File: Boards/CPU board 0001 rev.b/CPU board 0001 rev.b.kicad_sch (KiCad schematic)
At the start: 78 parts, among them J1 CEC card edge connector large, U10 7432, U11 7442, U12 7406, U13 7406, U14 7442, U15 7442, U16 M8216, U17 M8216, U18 6532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

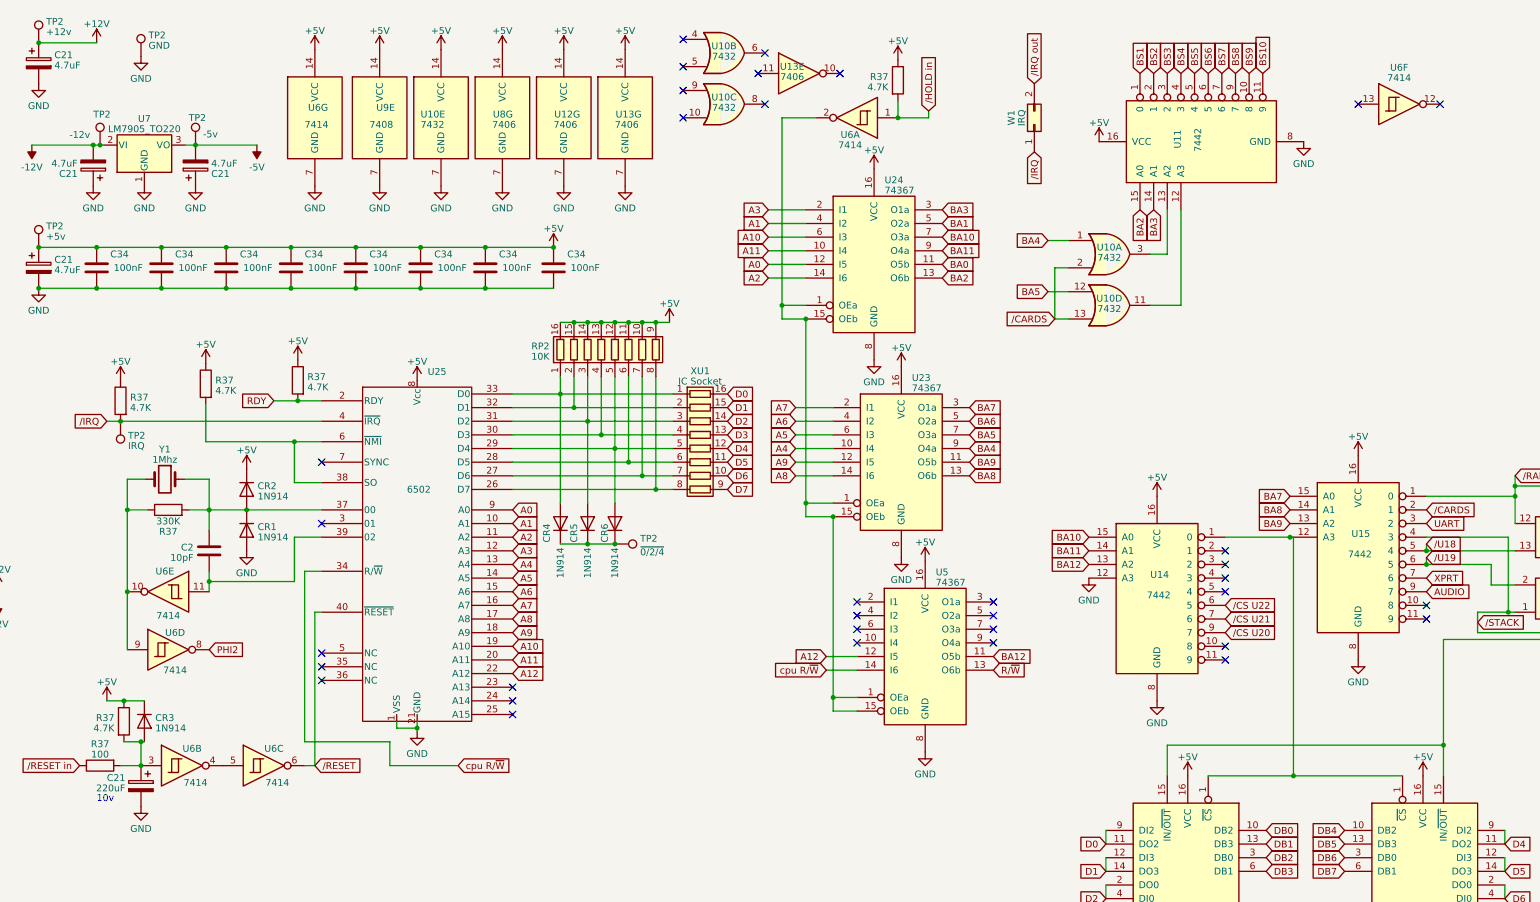
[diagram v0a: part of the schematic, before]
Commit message: checked Rev.c cpu board and tweaked copper on a and b
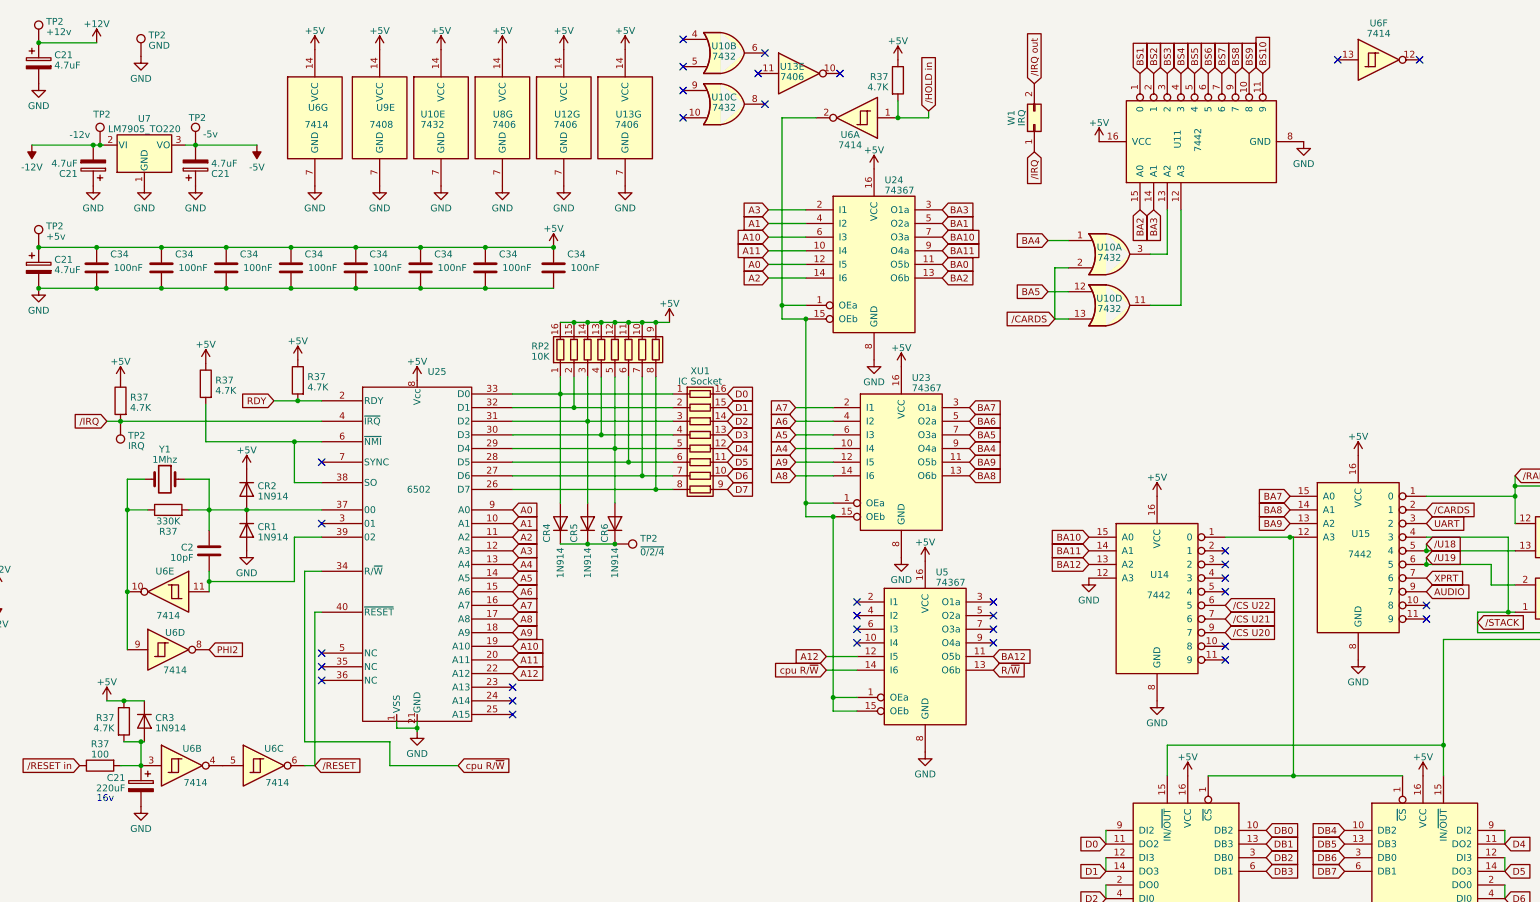
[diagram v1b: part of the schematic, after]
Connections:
- net at U18.18 (PB5): now also U12.3
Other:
- note added: "16v"
- note removed: "10v"
- moved on the sheet: U6F

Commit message: updated boards per real one
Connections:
- net at U18.18 (PB5): now also U12.3
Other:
- note added: "112 grounded on rev b schematic, not grounded on the rev b pcb"
- note added: "87 grounded on rev b schematic, not grounded on the rev b pcb"
- note removed: "112 grounded on rev a schematic, not grounded on the rev a pcb"
- note removed: "87 grounded on rev a schematic, not grounded on the rev a pcb"
- moved on the sheet: U6F
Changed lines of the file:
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@@
   (no_connect (at 170.815 203.835))
   (no_connect (at 419.1 185.42))
+  (no_connect (at 314.96 31.75))
   (no_connect (at 257.175 204.47))
   (no_connect (at 269.875 194.31))
   (no_connect (at 31.75 152.4))
+  (no_connect (at 330.2 31.75))
   (no_connect (at 44.45 142.24))
-  (no_connect (at 326.39 23.495))
   (no_connect (at 168.275 203.835))
   (no_connect (at 231.775 204.47))
@@
   (no_connect (at 44.45 175.26))
   (no_connect (at 175.895 193.675))
-  (no_connect (at 311.15 23.495))
   (no_connect (at 178.435 193.675))
   (no_connect (at 44.45 106.68))
@@
     (stroke (width 0) (type default))
   )
-  (text "112 grounded on rev a schematic, not grounded on the rev a pcb"
+  (text "112 grounded on rev b schematic, not grounded on the rev b pcb"
     (at -47.625 152.4 0)
     (effects (font (size 1.27 1.27)) (justify left bottom))
   )
-  (text "87 grounded on rev a schematic, not grounded on the rev a pcb"
+  (text "87 grounded on rev b schematic, not grounded on the rev b pcb"
     (at -46.99 89.535 0)
     (effects (font (size 1.27 1.27)) (justify left bottom))
@@
     )
   )
-  (symbol (lib_id "74xx:74LS14") (at 318.77 23.495 0) (unit 6)
+  (symbol (lib_id "74xx:74LS14") (at 322.58 31.75 0) (unit 6)
     (in_bom yes) (on_board yes) (dnp no) (fields_autoplaced)
-    (property "Reference" "U6" (at 318.77 16.6751 0)
+    (property "Reference" "U6" (at 322.58 24.9301 0)
       (effects (font (size 1.27 1.27)))
     )
-    (property "Value" "7414" (at 318.77 18.5961 0)
+    (property "Value" "7414" (at 322.58 26.8511 0)
       (effects (font (size 1.27 1.27)))
     )
-    (property "Footprint" "Package_DIP:DIP-14_W7.62mm" (at 318.77 23.495 0)
+    (property "Footprint" "Package_DIP:DIP-14_W7.62mm" (at 322.58 31.75 0)
       (effects (font (size 1.27 1.27)) hide)
     )
-    (property "Datasheet" "http://www.ti.com/lit/gpn/sn74LS14" (at 318.77 23.495 0)
+    (property "Datasheet" "http://www.ti.com/lit/gpn/sn74LS14" (at 322.58 31.75 0)
       (effects (font (size 1.27 1.27)) hide)
     )

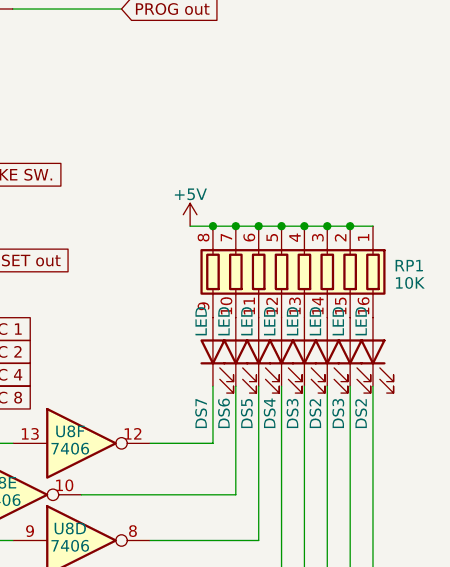
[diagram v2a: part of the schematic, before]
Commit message: revisions from real life boards
tip130a is actually tip30a, widened holes for crystal, widened holes for big power resistor, fixed cpu board LED resistors
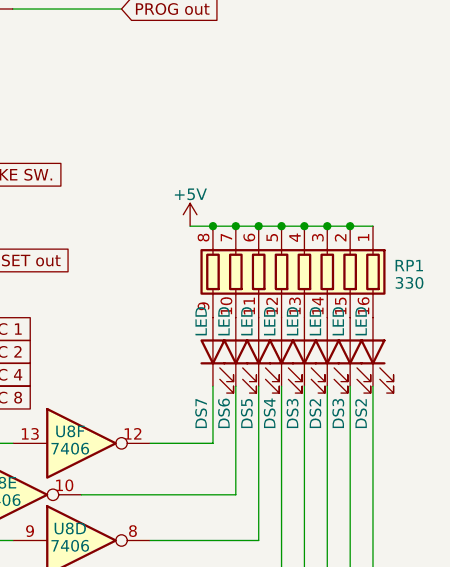
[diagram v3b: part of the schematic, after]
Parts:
- RP1: value 10K -> 330
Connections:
- net at U18.18 (PB5): now also U12.3
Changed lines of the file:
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@@
       (effects (font (size 1.27 1.27)) (justify left))
     )
-    (property "Value" "10K" (at 485.14 139.7 0)
+    (property "Value" "330" (at 485.14 139.7 0)
       (effects (font (size 1.27 1.27)) (justify left))
     )
